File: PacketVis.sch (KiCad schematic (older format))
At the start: 36 parts, among them J1 USB_B_Micro, J2 Conn_01x04, SW1 SW_Push_Dual, SW2 SW_SPST, SW3 SW_SPST, U1 3.3V 1A, U2 74HC595, U3 ESP-WROOM-02D

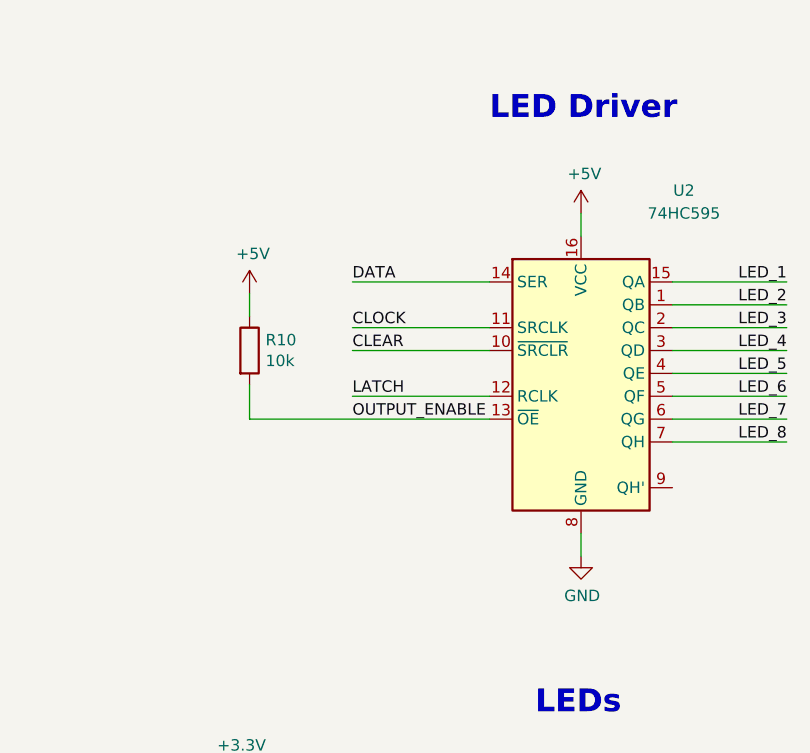
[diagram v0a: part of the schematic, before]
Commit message: Change Shift Register back to 3.3V
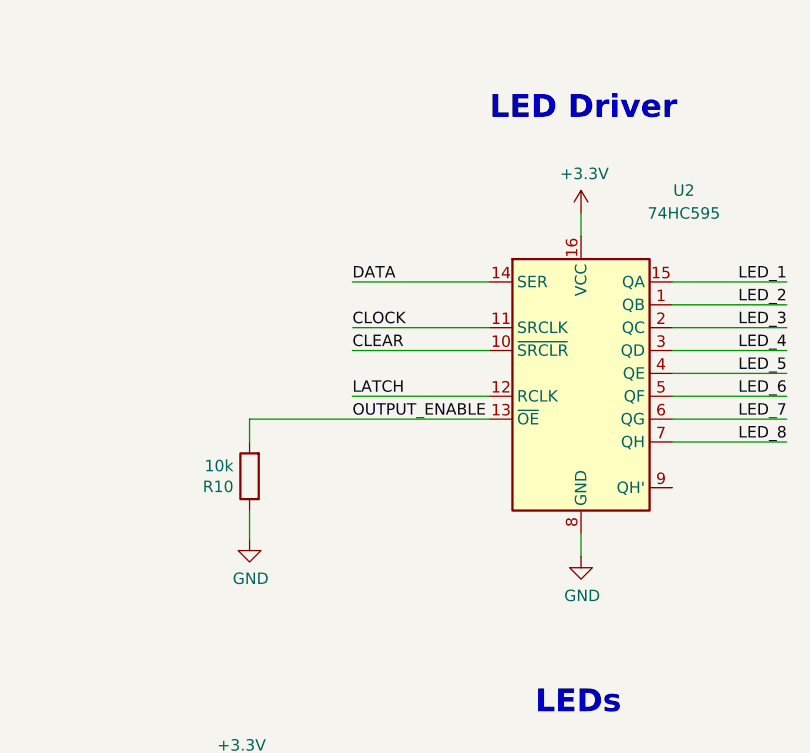
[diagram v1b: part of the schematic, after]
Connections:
- net +3V3: now also U2.16 (VCC)
- net +5V: no longer R10.1, U2.16 (VCC)
- net GND: now also R10.1
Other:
- moved on the sheet: R10
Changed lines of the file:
@@
 Wire Wire Line
 	3250 3800 3900 3800
-$Comp
-L Device:R R10
-U 1 1 5DD4919D
-P 7550 2100
-F 0 "R10" H 7620 2146 50  0000 L CNN
-F 1 "10k" H 7620 2055 50  0000 L CNN
-F 2 "Resistor_SMD:R_0805_2012Metric" V 7480 2100 50  0001 C CNN
-F 3 "~" H 7550 2100 50  0001 C CNN
-F 4 "RC0805JR-0710KL" H 7550 2100 50  0001 C CNN "Manufacturer PN"
-	1    7550 2100
-	1    0    0    -1
-$EndComp
-Wire Wire Line
-	7550 1850 7550 1950
-Wire Wire Line
-	7550 2400 7550 2250
 Wire Wire Line
 	7550 2400 8600 2400
@@
 	1    0    0    -1
 $EndComp
-$Comp
-L power:+5V #PWR0102
-U 1 1 5F41C719
+Wire Wire Line
+	9000 1500 9000 1600
+$Comp
+L power:+3.3V #PWR?
+U 1 1 5F6FB357
 P 9000 1500
-F 0 "#PWR0102" H 9000 1350 50  0001 C CNN
-F 1 "+5V" H 9015 1673 50  0000 C CNN
+F 0 "#PWR?" H 9000 1350 50  0001 C CNN
+F 1 "+3.3V" H 9015 1673 50  0000 C CNN
 F 2 "" H 9000 1500 50  0001 C CNN
 F 3 "" H 9000 1500 50  0001 C CNN
@@
 $EndComp
 $Comp
-L power:+5V #PWR0103
-U 1 1 5F41D0EC
-P 7550 1850
-F 0 "#PWR0103" H 7550 1700 50  0001 C CNN
-F 1 "+5V" H 7565 2023 50  0000 C CNN
-F 2 "" H 7550 1850 50  0001 C CNN
-F 3 "" H 7550 1850 50  0001 C CNN
-	1    7550 1850
-	1    0    0    -1
-$EndComp
-Wire Wire Line
-	9000 1500 9000 1600
+L Device:R R10
+U 1 1 5DD4919D
+P 7550 2650
+F 0 "R10" H 7620 2696 50  0000 L CNN
+F 1 "10k" H 7620 2605 50  0000 L CNN
+F 2 "Resistor_SMD:R_0805_2012Metric" V 7480 2650 50  0001 C CNN
+F 3 "~" H 7550 2650 50  0001 C CNN
+F 4 "RC0805JR-0710KL" H 7550 2650 50  0001 C CNN "Manufacturer PN"
+	1    7550 2650
+	-1   0    0    1
+$EndComp
+Wire Wire Line
+	7550 2500 7550 2400
+$Comp
+L power:GND #PWR?
+U 1 1 5F7093E8
+P 7550 2925
+F 0 "#PWR?" H 7550 2675 50  0001 C CNN
+F 1 "GND" H 7555 2752 50  0000 C CNN
+F 2 "" H 7550 2925 50  0001 C CNN
+F 3 "" H 7550 2925 50  0001 C CNN
+	1    7550 2925
+	1    0    0    -1
+$EndComp
+Wire Wire Line
+	7550 2800 7550 2925
 $EndSCHEMATC
